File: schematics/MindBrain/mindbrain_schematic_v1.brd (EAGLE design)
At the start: 92.4 x 49.5 mm, 49 parts, among them CON1 POWER, IC1 TL084P, IC2 TL084P

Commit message: added ground pour
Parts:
- moved OUTPUT1 5.08 mm to (85.1, 16.5)
- moved OUTPUT2 5.08 mm to (85.1, 19.1)
- moved OUTPUT3 5.08 mm to (85.1, 21.6)
- moved OUTPUT4 5.08 mm to (85.1, 24.1)
- moved OUTPUT5 5.08 mm to (85.1, 26.7)
- moved OUTPUT6 5.08 mm to (85.1, 29.2)
- moved OUTPUT7 5.08 mm to (85.1, 31.8)
- moved OUTPUT8 5.08 mm to (85.1, 34.3)
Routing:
- added copper zone on layer 1, net GND
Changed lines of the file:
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@@
 <element name="INPUT7" library="SparkFun-Connectors" package="1X01NS-KIT" value="" x="26.67" y="31.75"/>
 <element name="INPUT8" library="SparkFun-Connectors" package="1X01NS-KIT" value="" x="26.67" y="34.29" rot="R90"/>
-<element name="OUTPUT1" library="SparkFun-Connectors" package="1X01NS-KIT" value="" x="80.01" y="16.51"/>
-<element name="OUTPUT2" library="SparkFun-Connectors" package="1X01NS-KIT" value="" x="80.01" y="19.05"/>
-<element name="OUTPUT3" library="SparkFun-Connectors" package="1X01NS-KIT" value="" x="80.01" y="21.59"/>
-<element name="OUTPUT4" library="SparkFun-Connectors" package="1X01NS-KIT" value="" x="80.01" y="24.13"/>
-<element name="OUTPUT5" library="SparkFun-Connectors" package="1X01NS-KIT" value="" x="80.01" y="26.67"/>
-<element name="OUTPUT6" library="SparkFun-Connectors" package="1X01NS-KIT" value="" x="80.01" y="29.21"/>
-<element name="OUTPUT7" library="SparkFun-Connectors" package="1X01NS-KIT" value="" x="80.01" y="31.75"/>
-<element name="OUTPUT8" library="SparkFun-Connectors" package="1X01NS-KIT" value="" x="80.01" y="34.29"/>
+<element name="OUTPUT1" library="SparkFun-Connectors" package="1X01NS-KIT" value="" x="85.09" y="16.51"/>
+<element name="OUTPUT2" library="SparkFun-Connectors" package="1X01NS-KIT" value="" x="85.09" y="19.05"/>
+<element name="OUTPUT3" library="SparkFun-Connectors" package="1X01NS-KIT" value="" x="85.09" y="21.59"/>
+<element name="OUTPUT4" library="SparkFun-Connectors" package="1X01NS-KIT" value="" x="85.09" y="24.13"/>
+<element name="OUTPUT5" library="SparkFun-Connectors" package="1X01NS-KIT" value="" x="85.09" y="26.67"/>
+<element name="OUTPUT6" library="SparkFun-Connectors" package="1X01NS-KIT" value="" x="85.09" y="29.21"/>
+<element name="OUTPUT7" library="SparkFun-Connectors" package="1X01NS-KIT" value="" x="85.09" y="31.75"/>
+<element name="OUTPUT8" library="SparkFun-Connectors" package="1X01NS-KIT" value="" x="85.09" y="34.29"/>
 <element name="R2" library="SparkFun-Passives" package="AXIAL-0.4" value="1KΩ" x="73.66" y="12.7" rot="R90"/>
 <element name="R1" library="SparkFun-Passives" package="AXIAL-0.4" value="1KΩ" x="60.96" y="12.7" rot="R90"/>
@@
 <contactref element="AUDIOCARD-GND" pad="1"/>
 <contactref element="OUTPUT-GND" pad="1"/>
-<wire x1="67.31" y1="36.957" x2="73.66" y2="43.18" width="0" layer="19" extent="1-1"/>
-<wire x1="69.85" y1="33.02" x2="67.31" y2="36.957" width="0" layer="19" extent="1-1"/>
-<wire x1="64.77" y1="33.02" x2="67.31" y2="36.957" width="0" layer="19" extent="1-1"/>
-<wire x1="60.96" y1="43.18" x2="67.31" y2="36.957" width="0" layer="19" extent="1-1"/>
-<wire x1="48.26" y1="43.18" x2="60.96" y2="43.18" width="0" layer="19" extent="1-1"/>
-<wire x1="41.91" y1="36.957" x2="48.26" y2="43.18" width="0" layer="19" extent="1-1"/>
-<wire x1="44.45" y1="33.02" x2="41.91" y2="36.957" width="0" layer="19" extent="1-1"/>
-<wire x1="39.37" y1="33.02" x2="41.91" y2="36.957" width="0" layer="19" extent="1-1"/>
+<polygon width="0.4064" layer="1">
+<vertex x="-0.635" y="50.165"/>
+<vertex x="92.71" y="50.165"/>
+<vertex x="92.71" y="-0.635"/>
+<vertex x="-0.635" y="-0.635"/>
+</polygon>
+<wire x1="1.27" y1="-1.27" x2="1.27" y2="-3.81" width="0" layer="19" extent="1-1"/>
+<wire x1="6.35" y1="21.59" x2="1.27" y2="-1.27" width="0" layer="19" extent="1-1"/>
 <wire x1="35.56" y1="43.18" x2="41.91" y2="36.957" width="0" layer="19" extent="1-1"/>
-<wire x1="69.85" y1="17.78" x2="69.85" y2="33.02" width="0" layer="19" extent="1-1"/>
-<wire x1="67.31" y1="13.843" x2="69.85" y2="17.78" width="0" layer="19" extent="1-1"/>
-<wire x1="64.77" y1="17.78" x2="67.31" y2="13.843" width="0" layer="19" extent="1-1"/>
-<wire x1="73.66" y1="7.62" x2="67.31" y2="13.843" width="0" layer="19" extent="1-1"/>
-<wire x1="60.96" y1="7.62" x2="67.31" y2="13.843" width="0" layer="19" extent="1-1"/>
 <wire x1="48.26" y1="7.62" x2="60.96" y2="7.62" width="0" layer="19" extent="1-1"/>
 <wire x1="41.91" y1="13.843" x2="48.26" y2="7.62" width="0" layer="19" extent="1-1"/>
-<wire x1="44.45" y1="17.78" x2="41.91" y2="13.843" width="0" layer="19" extent="1-1"/>
-<wire x1="39.37" y1="17.78" x2="41.91" y2="13.843" width="0" layer="19" extent="1-1"/>
 <wire x1="35.56" y1="7.62" x2="41.91" y2="13.843" width="0" layer="19" extent="1-1"/>
-<wire x1="8.89" y1="21.59" x2="39.37" y2="17.78" width="0" layer="19" extent="1-1"/>
-<wire x1="8.89" y1="24.13" x2="8.89" y2="21.59" width="0" layer="19" extent="1-1"/>
-<wire x1="8.89" y1="26.67" x2="8.89" y2="24.13" width="0" layer="19" extent="1-1"/>
-<wire x1="1.27" y1="-1.27" x2="6.35" y2="21.59" width="0" layer="19" extent="1-1"/>
-<wire x1="1.27" y1="-3.81" x2="1.27" y2="-1.27" width="0" layer="19" extent="1-1"/>
 </signal>
 <signal name="N$2">
@@
 <contactref element="RF1" pad="P$2"/>
 <contactref element="IC1" pad="1"/>
-<wire x1="59.69" y1="21.59" x2="80.01" y2="16.51" width="0" layer="19" extent="1-1"/>
 <wire x1="58.42" y1="7.62" x2="56.515" y2="9.525" width="0.4064" layer="1"/>
 <wire x1="56.515" y1="9.525" x2="56.515" y2="19.05" width="0.4064" layer="1"/>
 <wire x1="56.515" y1="19.05" x2="59.055" y2="21.59" width="0.4064" layer="1"/>
 <wire x1="59.055" y1="21.59" x2="59.69" y2="21.59" width="0.4064" layer="1"/>
+<wire x1="59.69" y1="21.59" x2="85.09" y2="16.51" width="0" layer="19" extent="1-1"/>
 </signal>
 <signal name="N$3">
@@
 <wire x1="78.105" y1="19.05" x2="75.565" y2="21.59" width="0.4064" layer="1"/>
 <wire x1="75.565" y1="21.59" x2="74.93" y2="21.59" width="0.4064" layer="1"/>
-<wire x1="78.105" y1="19.05" x2="80.01" y2="19.05" width="0" layer="19" extent="1-1"/>
+<wire x1="78.105" y1="19.05" x2="85.09" y2="19.05" width="0" layer="19" extent="1-1"/>
 </signal>
 <signal name="N$6">
@@
 <contactref element="RF3" pad="P$2"/>
 <contactref element="IC1" pad="8"/>
-<wire x1="80.01" y1="21.59" x2="74.93" y2="29.21" width="0" layer="19" extent="1-1"/>
 <wire x1="76.2" y1="43.18" x2="78.105" y2="41.275" width="0.4064" layer="1"/>
 <wire x1="78.105" y1="41.275" x2="78.105" y2="31.75" width="0.4064" layer="1"/>
 <wire x1="78.105" y1="31.75" x2="75.565" y2="29.21" width="0.4064" layer="1"/>
 <wire x1="75.565" y1="29.21" x2="74.93" y2="29.21" width="0.4064" layer="1"/>
+<wire x1="75.565" y1="29.21" x2="85.09" y2="21.59" width="0" layer="19" extent="1-1"/>
 </signal>
 <signal name="N$9">
@@
 <contactref element="RF4" pad="P$2"/>
 <contactref element="IC1" pad="14"/>
-<wire x1="59.69" y1="29.21" x2="80.01" y2="24.13" width="0" layer="19" extent="1-1"/>
 <wire x1="58.42" y1="43.18" x2="56.515" y2="41.275" width="0.4064" layer="1"/>
 <wire x1="56.515" y1="41.275" x2="56.515" y2="31.75" width="0.4064" layer="1"/>
 <wire x1="56.515" y1="31.75" x2="59.055" y2="29.21" width="0.4064" layer="1"/>
 <wire x1="59.055" y1="29.21" x2="59.69" y2="29.21" width="0.4064" layer="1"/>
+<wire x1="59.69" y1="29.21" x2="85.09" y2="24.13" width="0" layer="19" extent="1-1"/>
 </signal>
 <signal name="N$12">
@@
 <contactref element="RF5" pad="P$2"/>
 <contactref element="IC2" pad="1"/>
-<wire x1="34.29" y1="21.59" x2="80.01" y2="26.67" width="0" layer="19" extent="1-1"/>
 <wire x1="33.02" y1="7.62" x2="31.115" y2="9.525" width="0.4064" layer="1"/>
 <wire x1="31.115" y1="9.525" x2="31.115" y2="19.05" width="0.4064" layer="1"/>
 <wire x1="31.115" y1="19.05" x2="33.655" y2="21.59" width="0.4064" layer="1"/>
 <wire x1="33.655" y1="21.59" x2="34.29" y2="21.59" width="0.4064" layer="1"/>
+<wire x1="34.29" y1="21.59" x2="85.09" y2="26.67" width="0" layer="19" extent="1-1"/>
 </signal>
 <signal name="N$15">
@@
 <contactref element="RF6" pad="P$2"/>
 <contactref element="IC2" pad="7"/>
-<wire x1="49.53" y1="21.59" x2="80.01" y2="29.21" width="0" layer="19" extent="1-1"/>
 <wire x1="50.8" y1="7.62" x2="52.705" y2="9.525" width="0.4064" layer="1"/>
 <wire x1="52.705" y1="9.525" x2="52.705" y2="19.05" width="0.4064" layer="1"/>
 <wire x1="52.705" y1="19.05" x2="50.165" y2="21.59" width="0.4064" layer="1"/>
 <wire x1="50.165" y1="21.59" x2="49.53" y2="21.59" width="0.4064" layer="1"/>
+<wire x1="52.705" y1="19.05" x2="85.09" y2="29.21" width="0" layer="19" extent="1-1"/>
 </signal>
 <signal name="N$18">
@@
 <contactref element="RF7" pad="P$2"/>
 <contactref element="IC2" pad="8"/>
-<wire x1="49.53" y1="29.21" x2="80.01" y2="31.75" width="0" layer="19" extent="1-1"/>
 <wire x1="50.8" y1="43.18" x2="52.705" y2="41.275" width="0.4064" layer="1"/>
 <wire x1="52.705" y1="41.275" x2="52.705" y2="31.75" width="0.4064" layer="1"/>
 <wire x1="52.705" y1="31.75" x2="50.165" y2="29.21" width="0.4064" layer="1"/>
 <wire x1="50.165" y1="29.21" x2="49.53" y2="29.21" width="0.4064" layer="1"/>
+<wire x1="52.705" y1="31.75" x2="85.09" y2="31.75" width="0" layer="19" extent="1-1"/>
 </signal>
 <signal name="N$21">
@@
 <contactref element="RF8" pad="P$2"/>
 <contactref element="IC2" pad="14"/>
-<wire x1="34.29" y1="29.21" x2="80.01" y2="34.29" width="0" layer="19" extent="1-1"/>
 <wire x1="33.02" y1="43.18" x2="31.115" y2="41.275" width="0.4064" layer="1"/>
 <wire x1="31.115" y1="41.275" x2="31.115" y2="31.75" width="0.4064" layer="1"/>
 <wire x1="31.115" y1="31.75" x2="33.655" y2="29.21" width="0.4064" layer="1"/>
 <wire x1="33.655" y1="29.21" x2="34.29" y2="29.21" width="0.4064" layer="1"/>
+<wire x1="34.29" y1="29.21" x2="85.09" y2="34.29" width="0" layer="19" extent="1-1"/>
 </signal>
 <signal name="N$24">

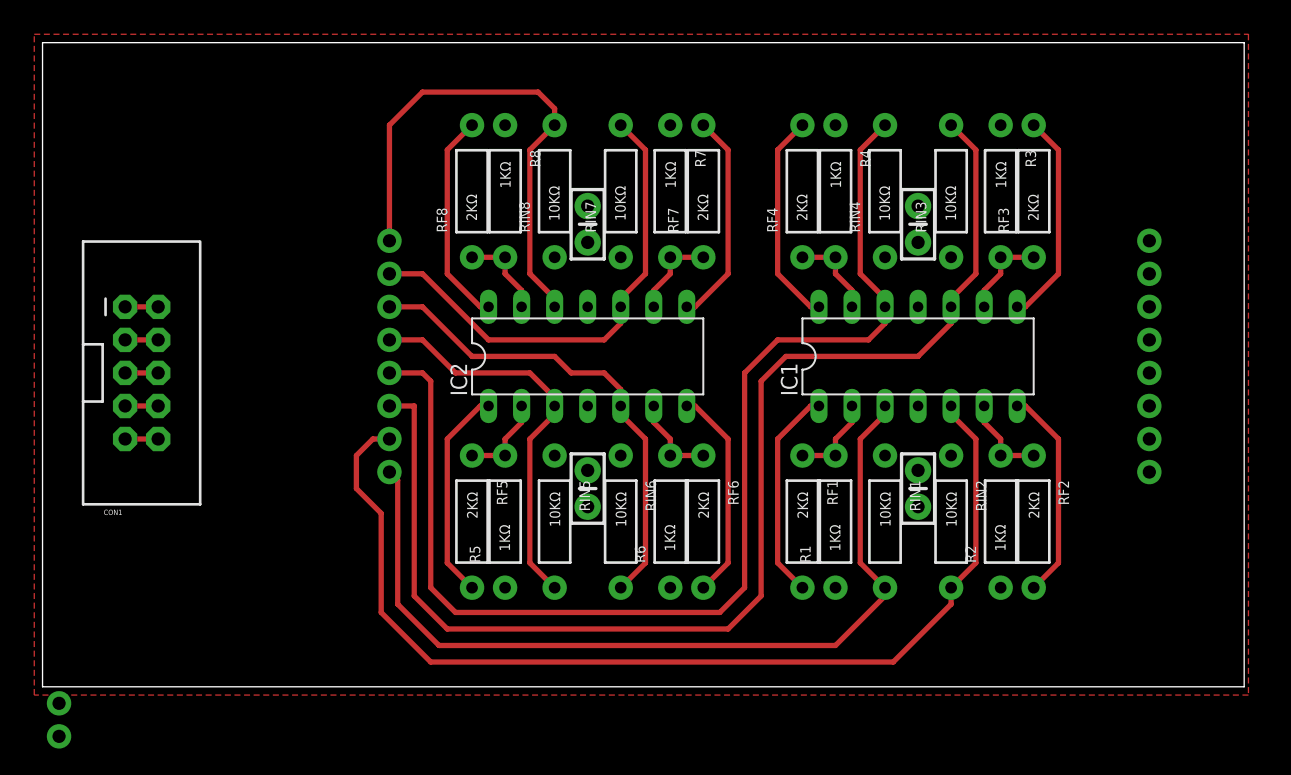
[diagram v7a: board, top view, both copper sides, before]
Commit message: routed +/- power bottomside
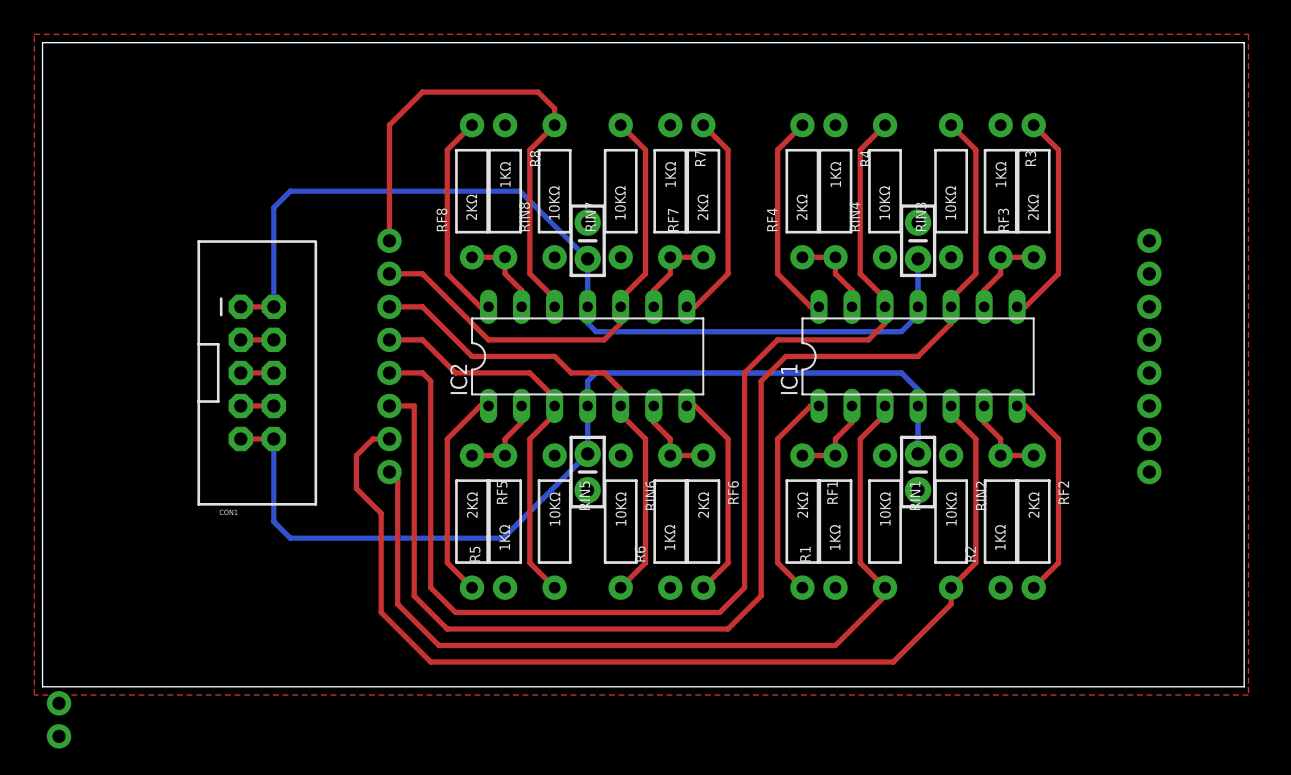
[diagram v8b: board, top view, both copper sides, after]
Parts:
- moved CON1 8.89 mm to (16.5, 24.1)
- moved C2 1.27 mm to (67.3, 34.3)
- moved C4 1.27 mm to (41.9, 34.3)
- moved C1 1.27 mm to (41.9, 16.5)
- moved C3 1.27 mm to (67.3, 16.5)
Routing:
- net N$25: track 2.54 -> 73.0 mm
- net N$27: track 2.54 -> 72.4 mm
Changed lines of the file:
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@@
 <element name="RIN7" library="SparkFun-Passives" package="AXIAL-0.4" value="10KΩ" x="44.45" y="38.1" rot="R90"/>
 <element name="RIN8" library="SparkFun-Passives" package="AXIAL-0.4" value="10KΩ" x="39.37" y="38.1" rot="R90"/>
-<element name="C1" library="SparkFun-Capacitors" package="CAP-PTH-SMALL-KIT" value="0.1uF" x="41.91" y="15.24" rot="R270"/>
-<element name="C2" library="SparkFun-Capacitors" package="CAP-PTH-SMALL-KIT" value="0.1uF" x="67.31" y="35.56" rot="R90"/>
-<element name="C3" library="SparkFun-Capacitors" package="CAP-PTH-SMALL-KIT" value="0.1uF" x="67.31" y="15.24" rot="R270"/>
-<element name="C4" library="SparkFun-Capacitors" package="CAP-PTH-SMALL-KIT" value="0.1uF" x="41.91" y="35.56" rot="R90"/>
-<element name="CON1" library="SparkFun-Connectors" package="2X5-SHROUDED" value="POWER" x="7.62" y="24.13"/>
+<element name="C1" library="SparkFun-Capacitors" package="CAP-PTH-SMALL-KIT" value="0.1uF" x="41.91" y="16.51" rot="R270"/>
+<element name="C2" library="SparkFun-Capacitors" package="CAP-PTH-SMALL-KIT" value="0.1uF" x="67.31" y="34.29" rot="R90"/>
+<element name="C3" library="SparkFun-Capacitors" package="CAP-PTH-SMALL-KIT" value="0.1uF" x="67.31" y="16.51" rot="R270"/>
+<element name="C4" library="SparkFun-Capacitors" package="CAP-PTH-SMALL-KIT" value="0.1uF" x="41.91" y="34.29" rot="R90"/>
+<element name="CON1" library="SparkFun-Connectors" package="2X5-SHROUDED" value="POWER" x="16.51" y="24.13"/>
 <element name="AUDIOCARD-GND" library="SparkFun-Connectors" package="1X01NS-KIT" value="" x="1.27" y="-1.27"/>
 <element name="OUTPUT-GND" library="SparkFun-Connectors" package="1X01NS-KIT" value="" x="1.27" y="-3.81"/>
@@
 <contactref element="C1" pad="2"/>
 <contactref element="C3" pad="2"/>
-<wire x1="6.35" y1="21.59" x2="8.89" y2="21.59" width="0.4064" layer="1"/>
-<wire x1="6.35" y1="26.67" x2="8.89" y2="26.67" width="0.4064" layer="1"/>
-<wire x1="6.35" y1="24.13" x2="8.89" y2="24.13" width="0.4064" layer="1"/>
+<wire x1="15.24" y1="21.59" x2="17.78" y2="21.59" width="0.4064" layer="1"/>
+<wire x1="15.24" y1="26.67" x2="17.78" y2="26.67" width="0.4064" layer="1"/>
+<wire x1="15.24" y1="24.13" x2="17.78" y2="24.13" width="0.4064" layer="1"/>
 <contactref element="AUDIOCARD-GND" pad="1"/>
 <contactref element="OUTPUT-GND" pad="1"/>
@@
 </polygon>
 <wire x1="1.27" y1="-1.27" x2="1.27" y2="-3.81" width="0" layer="19" extent="1-1"/>
-<wire x1="6.35" y1="21.59" x2="1.27" y2="-1.27" width="0" layer="19" extent="1-1"/>
-<wire x1="35.56" y1="43.18" x2="41.91" y2="36.957" width="0" layer="19" extent="1-1"/>
+<wire x1="15.24" y1="21.59" x2="1.27" y2="-1.27" width="0" layer="19" extent="1-1"/>
+<wire x1="35.56" y1="43.18" x2="41.91" y2="35.687" width="0" layer="19" extent="1-1"/>
 <wire x1="48.26" y1="7.62" x2="60.96" y2="7.62" width="0" layer="19" extent="1-1"/>
-<wire x1="41.91" y1="13.843" x2="48.26" y2="7.62" width="0" layer="19" extent="1-1"/>
-<wire x1="35.56" y1="7.62" x2="41.91" y2="13.843" width="0" layer="19" extent="1-1"/>
+<wire x1="41.91" y1="15.113" x2="48.26" y2="7.62" width="0" layer="19" extent="1-1"/>
+<wire x1="35.56" y1="7.62" x2="41.91" y2="15.113" width="0" layer="19" extent="1-1"/>
 </signal>
 <signal name="N$2">
@@
 <contactref element="C2" pad="1"/>
 <contactref element="C4" pad="1"/>
-<wire x1="6.35" y1="29.21" x2="8.89" y2="29.21" width="0.4064" layer="1"/>
-<wire x1="67.31" y1="29.21" x2="67.31" y2="34.163" width="0" layer="19" extent="1-1"/>
-<wire x1="41.91" y1="34.163" x2="67.31" y2="34.163" width="0" layer="19" extent="1-1"/>
-<wire x1="41.91" y1="29.21" x2="41.91" y2="34.163" width="0" layer="19" extent="1-1"/>
-<wire x1="8.89" y1="29.21" x2="41.91" y2="29.21" width="0" layer="19" extent="1-1"/>
+<wire x1="15.24" y1="29.21" x2="17.78" y2="29.21" width="0.4064" layer="1"/>
+<wire x1="17.78" y1="29.21" x2="17.78" y2="36.83" width="0.4064" layer="16"/>
+<wire x1="17.78" y1="36.83" x2="19.05" y2="38.1" width="0.4064" layer="16"/>
+<wire x1="19.05" y1="38.1" x2="36.703" y2="38.1" width="0.4064" layer="16"/>
+<wire x1="36.703" y1="38.1" x2="41.91" y2="32.893" width="0.4064" layer="16"/>
+<wire x1="41.91" y1="29.21" x2="41.91" y2="32.893" width="0.4064" layer="16"/>
+<wire x1="67.31" y1="29.21" x2="67.31" y2="32.893" width="0.4064" layer="16"/>
+<wire x1="67.31" y1="29.21" x2="67.31" y2="28.575" width="0.4064" layer="16"/>
+<wire x1="67.31" y1="28.575" x2="66.04" y2="27.305" width="0.4064" layer="16"/>
+<wire x1="66.04" y1="27.305" x2="42.545" y2="27.305" width="0.4064" layer="16"/>
+<wire x1="42.545" y1="27.305" x2="41.91" y2="27.94" width="0.4064" layer="16"/>
+<wire x1="41.91" y1="27.94" x2="41.91" y2="29.21" width="0.4064" layer="16"/>
 </signal>
 <signal name="N$25">
@@
 <contactref element="C3" pad="1"/>
 <contactref element="CON1" pad="10"/>
-<wire x1="6.35" y1="19.05" x2="8.89" y2="19.05" width="0.4064" layer="1"/>
-<wire x1="67.31" y1="16.637" x2="67.31" y2="21.59" width="0" layer="19" extent="1-1"/>
-<wire x1="41.91" y1="21.59" x2="67.31" y2="21.59" width="0" layer="19" extent="1-1"/>
-<wire x1="41.91" y1="16.637" x2="41.91" y2="21.59" width="0" layer="19" extent="1-1"/>
-<wire x1="8.89" y1="19.05" x2="41.91" y2="21.59" width="0" layer="19" extent="1-1"/>
+<wire x1="15.24" y1="19.05" x2="17.78" y2="19.05" width="0.4064" layer="1"/>
+<wire x1="17.78" y1="19.05" x2="17.78" y2="12.7" width="0.4064" layer="16"/>
+<wire x1="17.78" y1="12.7" x2="19.05" y2="11.43" width="0.4064" layer="16"/>
+<wire x1="19.05" y1="11.43" x2="35.433" y2="11.43" width="0.4064" layer="16"/>
+<wire x1="35.433" y1="11.43" x2="41.91" y2="17.907" width="0.4064" layer="16"/>
+<wire x1="41.91" y1="17.907" x2="41.91" y2="21.59" width="0.4064" layer="16"/>
+<wire x1="67.31" y1="17.907" x2="67.31" y2="21.59" width="0.4064" layer="16"/>
+<wire x1="41.91" y1="21.59" x2="41.91" y2="23.495" width="0.4064" layer="16"/>
+<wire x1="41.91" y1="23.495" x2="42.545" y2="24.13" width="0.4064" layer="16"/>
+<wire x1="42.545" y1="24.13" x2="66.04" y2="24.13" width="0.4064" layer="16"/>
+<wire x1="66.04" y1="24.13" x2="67.31" y2="22.86" width="0.4064" layer="16"/>
+<wire x1="67.31" y1="22.86" x2="67.31" y2="21.59" width="0.4064" layer="16"/>
 </signal>
 </signals>
